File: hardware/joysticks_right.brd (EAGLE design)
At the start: 64.8 x 87.6 mm, 10 parts, among them IC1 MEGA16-M

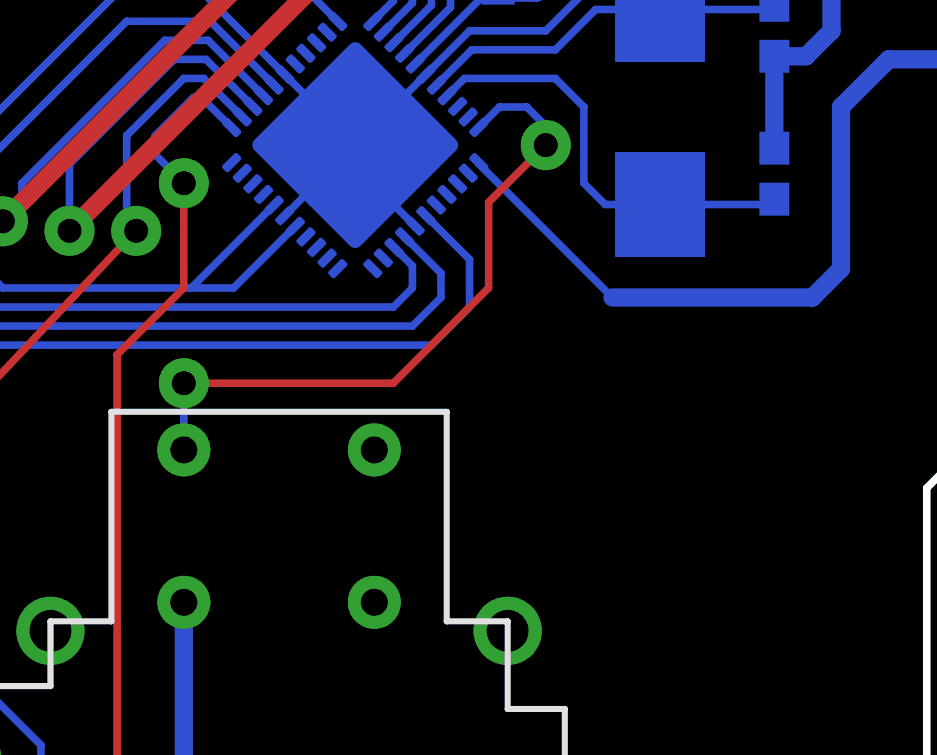
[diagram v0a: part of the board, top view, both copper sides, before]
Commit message: added mode selection jumper (SPI/I2C)
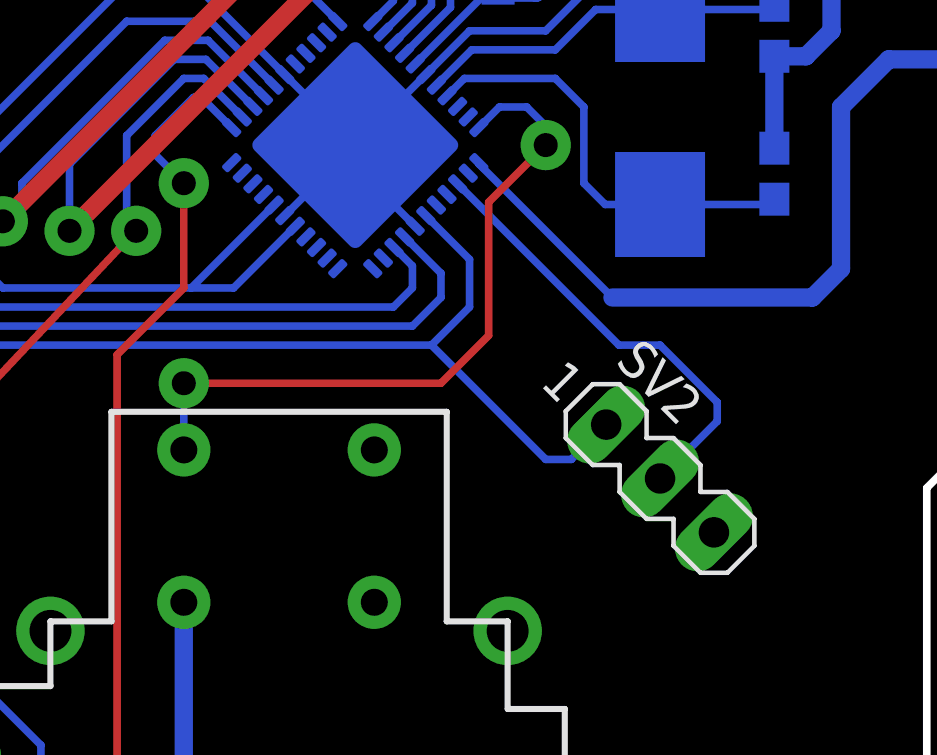
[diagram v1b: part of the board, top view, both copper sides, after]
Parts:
- added SV2: (no value), con-lstb:MA03-1
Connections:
- new net MD_SEL: IC1.14, SV2.2
- net GND: now also SV2.3
- net VCC: now also SV2.1
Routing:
- net MD_SEL: track 0.00 -> 15.0 mm
- net VCC: track 209.6 -> 217.4 mm
- net BUT_RB: track 22.7 -> 23.6 mm
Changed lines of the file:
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@@
 <element name="U$2" library="holes" package="3,0" value="" x="21.59" y="2.54"/>
 <element name="U$3" library="holes" package="3,0" value="" x="32.0675" y="77.47"/>
+<element name="SV2" library="con-lstb" package="MA03-1" value="" x="34.29" y="32.0675" rot="R315">
+<attribute name="OC_NEWARK" value="unknown" x="34.29" y="32.0675" size="1.778" layer="27" rot="R315" display="off"/>
+<attribute name="MPN" value="" x="34.29" y="32.0675" size="1.778" layer="27" rot="R315" display="off"/>
+<attribute name="MF" value="" x="34.29" y="32.0675" size="1.778" layer="27" rot="R315" display="off"/>
+<attribute name="OC_FARNELL" value="unknown" x="34.29" y="32.0675" size="1.778" layer="27" rot="R315" display="off"/>
+</element>
 </elements>
 <signals>
@@
 <vertex x="3.81" y="62.23"/>
 </polygon>
+<contactref element="SV2" pad="3"/>
 </signal>
 <signal name="VCC">
@@
 <wire x1="22.132425" y1="40.475315625" x2="20.074609375" y2="38.4175" width="0.254" layer="16"/>
 <wire x1="20.074609375" y1="38.4175" x2="18.660396875" y2="38.4175" width="0.254" layer="16"/>
+<contactref element="SV2" pad="1"/>
+<wire x1="32.493946875" y1="33.86355" x2="31.332896875" y2="32.7025" width="0.254" layer="16"/>
+<wire x1="31.332896875" y1="32.7025" x2="30.48" y2="32.7025" width="0.254" layer="16"/>
+<wire x1="30.48" y1="32.7025" x2="26.67" y2="36.5125" width="0.254" layer="16"/>
 </signal>
 <signal name="N$1">
@@
 <via x="30.48" y="43.18" extent="1-16" drill="0.8" diameter="1.6764"/>
 <wire x1="30.48" y1="43.18" x2="28.575" y2="41.275" width="0.254" layer="1"/>
-<wire x1="28.575" y1="41.275" x2="28.575" y2="38.4175" width="0.254" layer="1"/>
-<wire x1="28.575" y1="38.4175" x2="25.4" y2="35.2425" width="0.254" layer="1"/>
-<wire x1="25.4" y1="35.2425" x2="18.415" y2="35.2425" width="0.254" layer="1"/>
+<wire x1="28.575" y1="41.275" x2="28.575" y2="36.83" width="0.254" layer="1"/>
+<wire x1="28.575" y1="36.83" x2="26.9875" y2="35.2425" width="0.254" layer="1"/>
+<wire x1="26.9875" y1="35.2425" x2="18.415" y2="35.2425" width="0.254" layer="1"/>
 <via x="18.415" y="35.2425" extent="1-16" drill="0.8" diameter="1.6764"/>
 <wire x1="18.415" y1="35.2425" x2="18.415" y2="33.02" width="0.254" layer="16"/>
 </signal>
+<signal name="MD_SEL">
+<contactref element="IC1" pad="14"/>
+<contactref element="SV2" pad="2"/>
+<wire x1="27.541790625" y1="41.889528125" x2="32.91881875" y2="36.5125" width="0.254" layer="16"/>
+<wire x1="32.91881875" y1="36.5125" x2="34.29" y2="36.5125" width="0.254" layer="16"/>
+<wire x1="34.29" y1="36.5125" x2="36.195" y2="34.6075" width="0.254" layer="16"/>
+<wire x1="36.195" y1="34.6075" x2="36.195" y2="33.9725" width="0.254" layer="16"/>
+<wire x1="36.195" y1="33.9725" x2="34.29" y2="32.0675" width="0.254" layer="16"/>
+</signal>
 </signals>

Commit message: some tuning to the layout
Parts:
- moved SV2 0.90 mm to (34.9, 32.7)
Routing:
- net BUT_RB: track 23.6 -> 31.9 mm
- net JOY_RB_H: track 52.4 -> 55.5 mm
- net VCC: track 217.4 -> 218.3 mm
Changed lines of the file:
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@@
 <element name="U$2" library="holes" package="3,0" value="" x="21.59" y="2.54"/>
 <element name="U$3" library="holes" package="3,0" value="" x="32.0675" y="77.47"/>
-<element name="SV2" library="con-lstb" package="MA03-1" value="" x="34.29" y="32.0675" rot="R315">
-<attribute name="OC_NEWARK" value="unknown" x="34.29" y="32.0675" size="1.778" layer="27" rot="R315" display="off"/>
-<attribute name="MPN" value="" x="34.29" y="32.0675" size="1.778" layer="27" rot="R315" display="off"/>
-<attribute name="MF" value="" x="34.29" y="32.0675" size="1.778" layer="27" rot="R315" display="off"/>
-<attribute name="OC_FARNELL" value="unknown" x="34.29" y="32.0675" size="1.778" layer="27" rot="R315" display="off"/>
+<element name="SV2" library="con-lstb" package="MA03-1" value="" x="34.925" y="32.7025" rot="R315">
+<attribute name="OC_NEWARK" value="unknown" x="34.925" y="32.7025" size="1.778" layer="27" rot="R315" display="off"/>
+<attribute name="MPN" value="" x="34.925" y="32.7025" size="1.778" layer="27" rot="R315" display="off"/>
+<attribute name="MF" value="" x="34.925" y="32.7025" size="1.778" layer="27" rot="R315" display="off"/>
+<attribute name="OC_FARNELL" value="unknown" x="34.925" y="32.7025" size="1.778" layer="27" rot="R315" display="off"/>
 </element>
 </elements>
@@
 <wire x1="27.94" y1="39.37" x2="27.94" y2="37.7825" width="0.254" layer="16"/>
 <wire x1="27.94" y1="37.7825" x2="26.67" y2="36.5125" width="0.254" layer="16"/>
-<wire x1="26.67" y1="36.5125" x2="6.985" y2="36.5125" width="0.254" layer="16"/>
+<wire x1="26.67" y1="36.5125" x2="6.985" y2="36.5125" width="0.4064" layer="16"/>
 <wire x1="12.3825" y1="38.4175" x2="18.660396875" y2="38.4175" width="0.254" layer="16"/>
 <wire x1="18.660396875" y1="38.4175" x2="21.42531875" y2="41.182421875" width="0.254" layer="16"/>
@@
 <wire x1="20.074609375" y1="38.4175" x2="18.660396875" y2="38.4175" width="0.254" layer="16"/>
 <contactref element="SV2" pad="1"/>
-<wire x1="32.493946875" y1="33.86355" x2="31.332896875" y2="32.7025" width="0.254" layer="16"/>
-<wire x1="31.332896875" y1="32.7025" x2="30.48" y2="32.7025" width="0.254" layer="16"/>
-<wire x1="30.48" y1="32.7025" x2="26.67" y2="36.5125" width="0.254" layer="16"/>
+<wire x1="33.128946875" y1="34.49855" x2="31.332896875" y2="32.7025" width="0.4064" layer="16"/>
+<wire x1="31.332896875" y1="32.7025" x2="30.48" y2="32.7025" width="0.4064" layer="16"/>
+<wire x1="30.48" y1="32.7025" x2="26.67" y2="36.5125" width="0.4064" layer="16"/>
 </signal>
 <signal name="N$1">
@@
 <wire x1="18.7325" y1="44.7675" x2="17.4625" y2="43.4975" width="0.254" layer="16"/>
 <wire x1="17.4625" y1="43.4975" x2="17.4625" y2="42.8625" width="0.254" layer="16"/>
-<wire x1="21.59" y1="10.16" x2="21.59" y2="13.6525" width="0.254" layer="16"/>
-<wire x1="21.59" y1="13.6525" x2="18.7325" y2="16.51" width="0.254" layer="16"/>
-<wire x1="18.7325" y1="16.51" x2="12.7" y2="16.51" width="0.254" layer="16"/>
-<wire x1="12.7" y1="16.51" x2="12.065" y2="15.875" width="0.254" layer="16"/>
-<wire x1="12.065" y1="15.875" x2="10.795" y2="15.875" width="0.254" layer="16"/>
-<wire x1="10.795" y1="15.875" x2="10.16" y2="16.51" width="0.254" layer="16"/>
-<wire x1="10.16" y1="16.51" x2="10.16" y2="17.4625" width="0.254" layer="16"/>
-<wire x1="10.16" y1="17.4625" x2="10.4775" y2="17.78" width="0.254" layer="16"/>
-<wire x1="10.4775" y1="17.78" x2="13.0175" y2="17.78" width="0.254" layer="16"/>
+<wire x1="21.59" y1="10.16" x2="21.59" y2="13.6525" width="0.4064" layer="16"/>
+<wire x1="21.59" y1="13.6525" x2="19.05" y2="16.1925" width="0.4064" layer="16"/>
+<wire x1="19.05" y1="16.1925" x2="12.7" y2="16.1925" width="0.4064" layer="16"/>
+<wire x1="12.7" y1="16.1925" x2="12.065" y2="15.5575" width="0.4064" layer="16"/>
+<wire x1="12.065" y1="15.5575" x2="10.4775" y2="15.5575" width="0.4064" layer="16"/>
+<wire x1="10.4775" y1="15.5575" x2="9.8425" y2="16.1925" width="0.4064" layer="16"/>
+<wire x1="9.8425" y1="16.1925" x2="9.8425" y2="18.7325" width="0.4064" layer="16"/>
+<wire x1="9.8425" y1="18.7325" x2="10.16" y2="19.05" width="0.4064" layer="16"/>
+<wire x1="10.16" y1="19.05" x2="14.605" y2="19.05" width="0.254" layer="16"/>
 <wire x1="17.4625" y1="42.8625" x2="18.415" y2="41.91" width="0.254" layer="16"/>
 <via x="18.415" y="41.91" extent="1-16" drill="0.8" diameter="1.6764"/>
-<wire x1="18.415" y1="41.91" x2="18.415" y2="38.4175" width="0.254" layer="1"/>
-<wire x1="18.415" y1="38.4175" x2="16.1925" y2="36.195" width="0.254" layer="1"/>
-<wire x1="16.1925" y1="36.195" x2="16.1925" y2="20.955" width="0.254" layer="1"/>
-<via x="16.1925" y="20.955" extent="1-16" drill="0.8" diameter="1.4224"/>
-<wire x1="13.0175" y1="17.78" x2="16.1925" y2="20.955" width="0.254" layer="16"/>
+<wire x1="18.415" y1="41.91" x2="18.415" y2="38.4175" width="0.4064" layer="1"/>
+<wire x1="18.415" y1="38.4175" x2="14.605" y2="34.6075" width="0.4064" layer="1"/>
+<via x="14.605" y="34.6075" extent="1-16" drill="0.8" diameter="1.6764"/>
+<wire x1="14.605" y1="34.6075" x2="14.605" y2="33.3375" width="0.4064" layer="16"/>
+<wire x1="14.605" y1="33.3375" x2="16.1925" y2="31.75" width="0.4064" layer="16"/>
+<wire x1="16.1925" y1="31.75" x2="16.1925" y2="20.6375" width="0.4064" layer="16"/>
+<wire x1="16.1925" y1="20.6375" x2="14.605" y2="19.05" width="0.4064" layer="16"/>
 </signal>
 <signal name="JOY_RB_V">
@@
 <wire x1="16.51" y1="43.4975" x2="16.51" y2="40.64" width="0.254" layer="16"/>
 <wire x1="16.51" y1="40.64" x2="16.8275" y2="40.3225" width="0.254" layer="16"/>
-<wire x1="11.43" y1="25.4" x2="13.6525" y2="23.1775" width="0.254" layer="16"/>
-<wire x1="13.6525" y1="23.1775" x2="13.6525" y2="20.955" width="0.254" layer="16"/>
-<wire x1="13.6525" y1="20.955" x2="13.0175" y2="20.32" width="0.254" layer="16"/>
-<wire x1="13.0175" y1="20.32" x2="11.43" y2="20.32" width="0.254" layer="16"/>
+<wire x1="11.43" y1="25.4" x2="13.6525" y2="23.1775" width="0.4064" layer="16"/>
+<wire x1="13.6525" y1="23.1775" x2="13.6525" y2="20.955" width="0.4064" layer="16"/>
+<wire x1="13.6525" y1="20.955" x2="13.0175" y2="20.32" width="0.4064" layer="16"/>
+<wire x1="13.0175" y1="20.32" x2="11.43" y2="20.32" width="0.4064" layer="16"/>
 <via x="16.8275" y="40.3225" extent="1-16" drill="0.8" diameter="1.6764"/>
 <wire x1="16.8275" y1="40.3225" x2="16.51" y2="40.005" width="0.254" layer="1"/>
-<wire x1="16.51" y1="40.005" x2="11.43" y2="34.6075" width="0.254" layer="1"/>
+<wire x1="16.51" y1="40.005" x2="11.43" y2="34.6075" width="0.4064" layer="1"/>
 <via x="11.43" y="34.6075" extent="1-16" drill="0.8" diameter="1.6764"/>
-<wire x1="11.43" y1="34.6075" x2="11.43" y2="25.4" width="0.254" layer="16"/>
+<wire x1="11.43" y1="34.6075" x2="11.43" y2="25.4" width="0.4064" layer="16"/>
 </signal>
 <signal name="JOY_RT_H">
@@
 <wire x1="30.48" y1="43.815" x2="30.48" y2="43.18" width="0.254" layer="16"/>
 <via x="30.48" y="43.18" extent="1-16" drill="0.8" diameter="1.6764"/>
-<wire x1="30.48" y1="43.18" x2="28.575" y2="41.275" width="0.254" layer="1"/>
-<wire x1="28.575" y1="41.275" x2="28.575" y2="36.83" width="0.254" layer="1"/>
-<wire x1="28.575" y1="36.83" x2="26.9875" y2="35.2425" width="0.254" layer="1"/>
-<wire x1="26.9875" y1="35.2425" x2="18.415" y2="35.2425" width="0.254" layer="1"/>
-<via x="18.415" y="35.2425" extent="1-16" drill="0.8" diameter="1.6764"/>
-<wire x1="18.415" y1="35.2425" x2="18.415" y2="33.02" width="0.254" layer="16"/>
+<wire x1="30.48" y1="43.18" x2="30.7975" y2="42.8625" width="0.254" layer="1"/>
+<wire x1="30.7975" y1="42.8625" x2="30.7975" y2="31.4325" width="0.254" layer="1"/>
+<wire x1="30.7975" y1="31.4325" x2="32.0675" y2="30.1625" width="0.254" layer="1"/>
+<via x="32.0675" y="30.1625" extent="1-16" drill="0.8" diameter="1.6764"/>
+<wire x1="32.0675" y1="30.1625" x2="21.2725" y2="30.1625" width="0.4064" layer="16"/>
+<wire x1="21.2725" y1="30.1625" x2="18.415" y2="33.02" width="0.4064" layer="16"/>
 </signal>
 <signal name="MD_SEL">
 <contactref element="IC1" pad="14"/>
 <contactref element="SV2" pad="2"/>
-<wire x1="27.541790625" y1="41.889528125" x2="32.91881875" y2="36.5125" width="0.254" layer="16"/>
-<wire x1="32.91881875" y1="36.5125" x2="34.29" y2="36.5125" width="0.254" layer="16"/>
-<wire x1="34.29" y1="36.5125" x2="36.195" y2="34.6075" width="0.254" layer="16"/>
-<wire x1="36.195" y1="34.6075" x2="36.195" y2="33.9725" width="0.254" layer="16"/>
-<wire x1="36.195" y1="33.9725" x2="34.29" y2="32.0675" width="0.254" layer="16"/>
+<wire x1="27.541790625" y1="41.889528125" x2="32.60131875" y2="36.83" width="0.254" layer="16"/>
+<wire x1="32.60131875" y1="36.83" x2="34.6075" y2="36.83" width="0.254" layer="16"/>
+<wire x1="34.6075" y1="36.83" x2="36.5125" y2="34.925" width="0.254" layer="16"/>
+<wire x1="36.5125" y1="34.925" x2="36.5125" y2="34.29" width="0.254" layer="16"/>
+<wire x1="36.5125" y1="34.29" x2="34.925" y2="32.7025" width="0.254" layer="16"/>
 </signal>
 </signals>

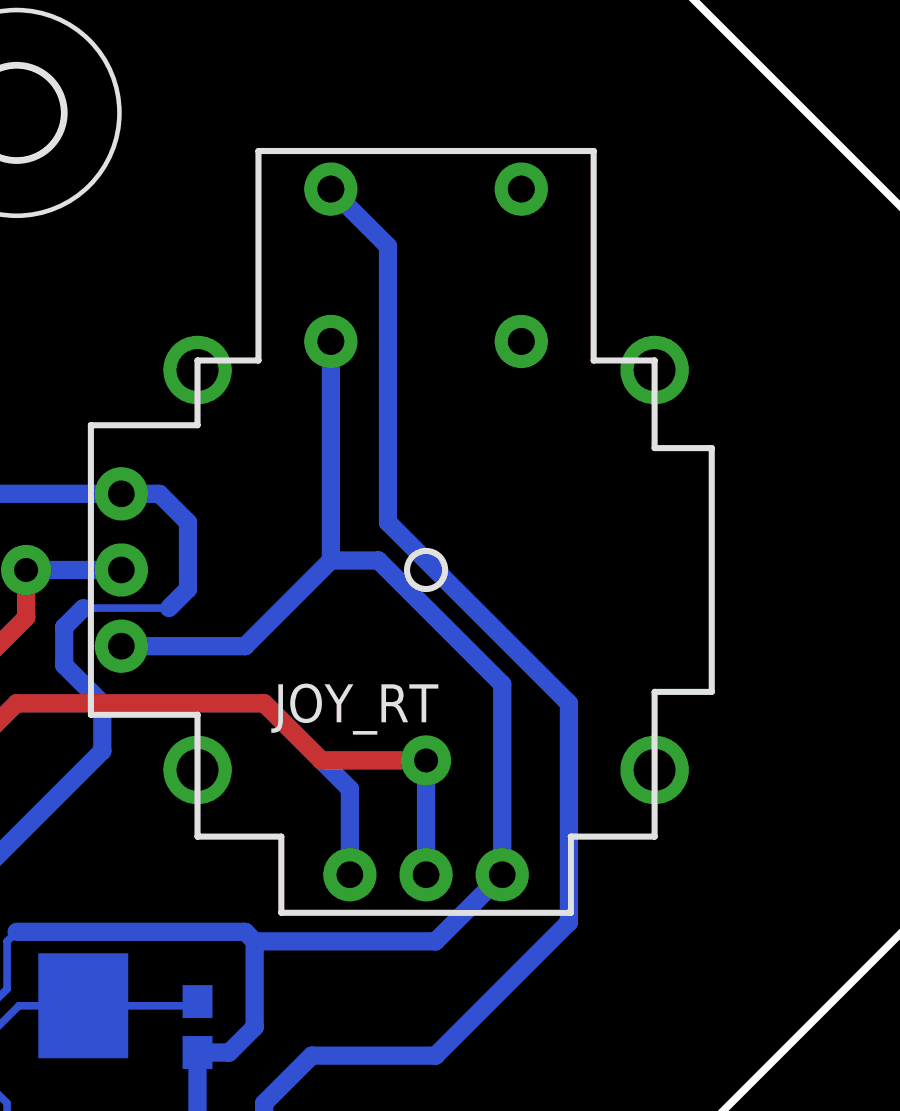
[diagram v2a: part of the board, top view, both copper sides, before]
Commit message: minor layout tuning due to etching fuckup
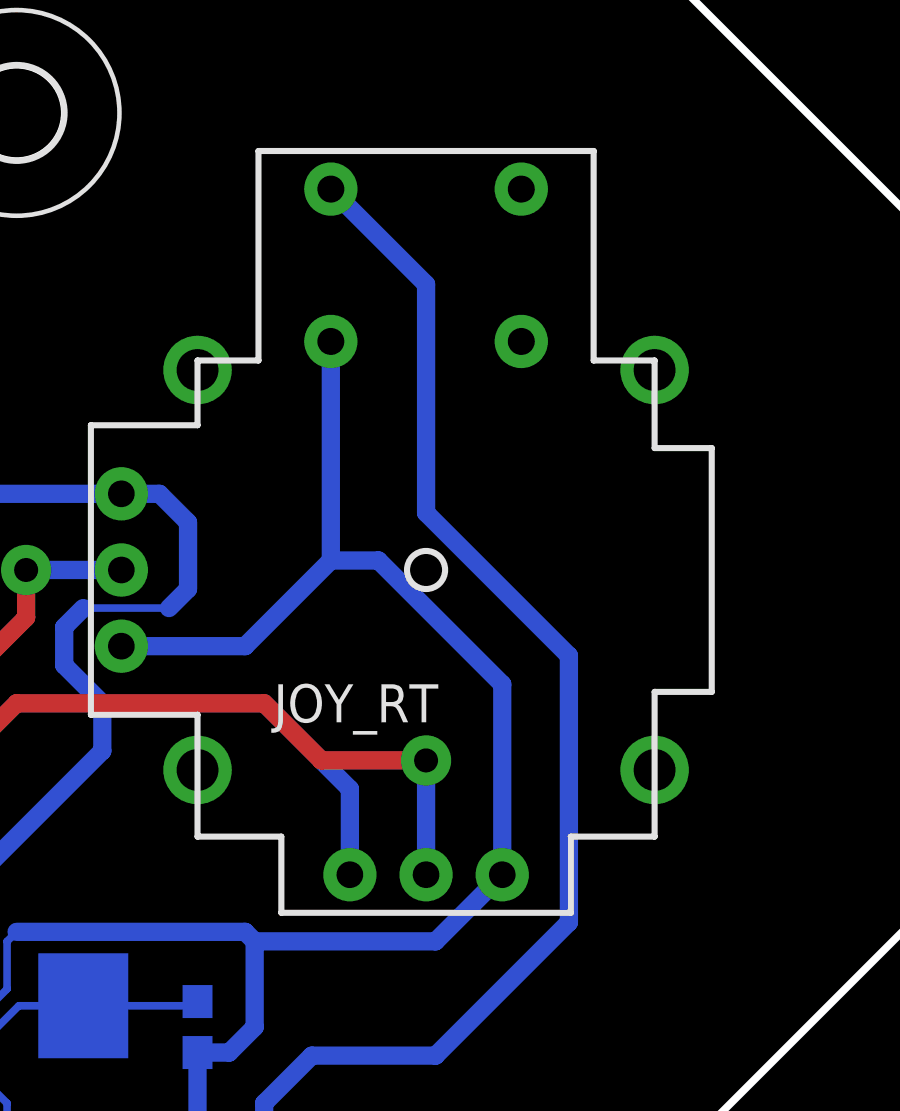
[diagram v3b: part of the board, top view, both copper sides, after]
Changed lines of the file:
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@@
 <wire x1="16.1925" y1="48.26" x2="19.05" y2="48.26" width="0.254" layer="16"/>
 <wire x1="19.05" y1="48.26" x2="21.778871875" y2="45.531128125" width="0.254" layer="16"/>
-<polygon width="0.254" layer="16" isolate="0.3048">
+<polygon width="0.254" layer="16" isolate="0.4064">
 <vertex x="-1.27" y="57.15"/>
 <vertex x="-1.27" y="34.29"/>
@@
 <contactref element="JOY_RT" pad="B1A"/>
 <contactref element="IC1" pad="12"/>
-<wire x1="42.545" y1="74.93" x2="44.45" y2="73.025" width="0.6096" layer="16"/>
-<wire x1="44.45" y1="73.025" x2="44.45" y2="63.8175" width="0.6096" layer="16"/>
-<wire x1="44.45" y1="63.8175" x2="50.4825" y2="57.785" width="0.6096" layer="16"/>
-<wire x1="50.4825" y1="57.785" x2="50.4825" y2="50.4825" width="0.6096" layer="16"/>
+<wire x1="42.545" y1="74.93" x2="45.72" y2="71.755" width="0.6096" layer="16"/>
+<wire x1="45.72" y1="71.755" x2="45.72" y2="64.135" width="0.6096" layer="16"/>
+<wire x1="45.72" y1="64.135" x2="50.4825" y2="59.3725" width="0.6096" layer="16"/>
+<wire x1="50.4825" y1="59.3725" x2="50.4825" y2="50.4825" width="0.6096" layer="16"/>
 <wire x1="50.4825" y1="50.4825" x2="46.0375" y2="46.0375" width="0.6096" layer="16"/>
 <wire x1="46.0375" y1="46.0375" x2="41.91" y2="46.0375" width="0.6096" layer="16"/>

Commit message: set value for xtal-caps
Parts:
- C1, C2: value (none) -> 18p
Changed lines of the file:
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@@
 </element>
 <element name="U$1" library="jocki" package="ABM2" value="CRYSTALABM2" x="34.29" y="44.45" rot="MR90"/>
-<element name="C1" library="rcl" package="C0603" value="" x="38.1" y="46.99" rot="MR90"/>
-<element name="C2" library="rcl" package="C0603" value="" x="38.1" y="42.2275" rot="MR270"/>
+<element name="C1" library="rcl" package="C0603" value="18p" x="38.1" y="46.99" rot="MR90"/>
+<element name="C2" library="rcl" package="C0603" value="18p" x="38.1" y="42.2275" rot="MR270"/>
 <element name="SV1" library="con-lstb" package="MA05-2" value="" x="7.62" y="45.72" rot="R270">
 <attribute name="OC_NEWARK" value="unknown" x="-25.4" y="-1.27" size="1.778" layer="27" rot="R270" display="off"/>
